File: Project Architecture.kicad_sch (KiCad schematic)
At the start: 0 parts

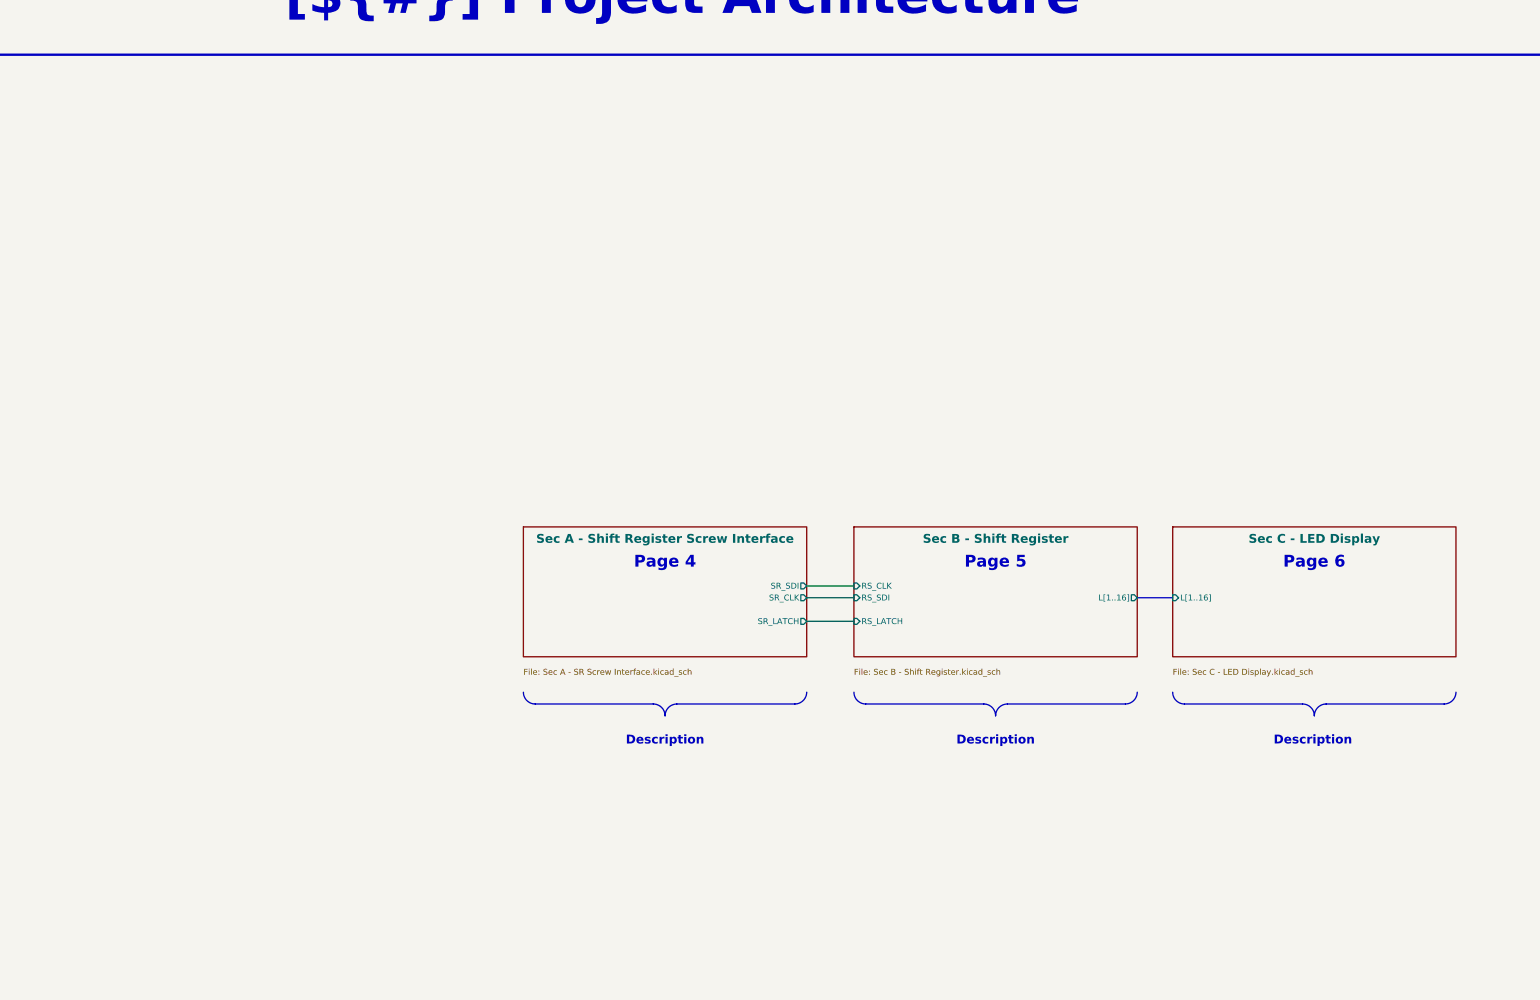
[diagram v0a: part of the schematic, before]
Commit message: documentation update / block diagram
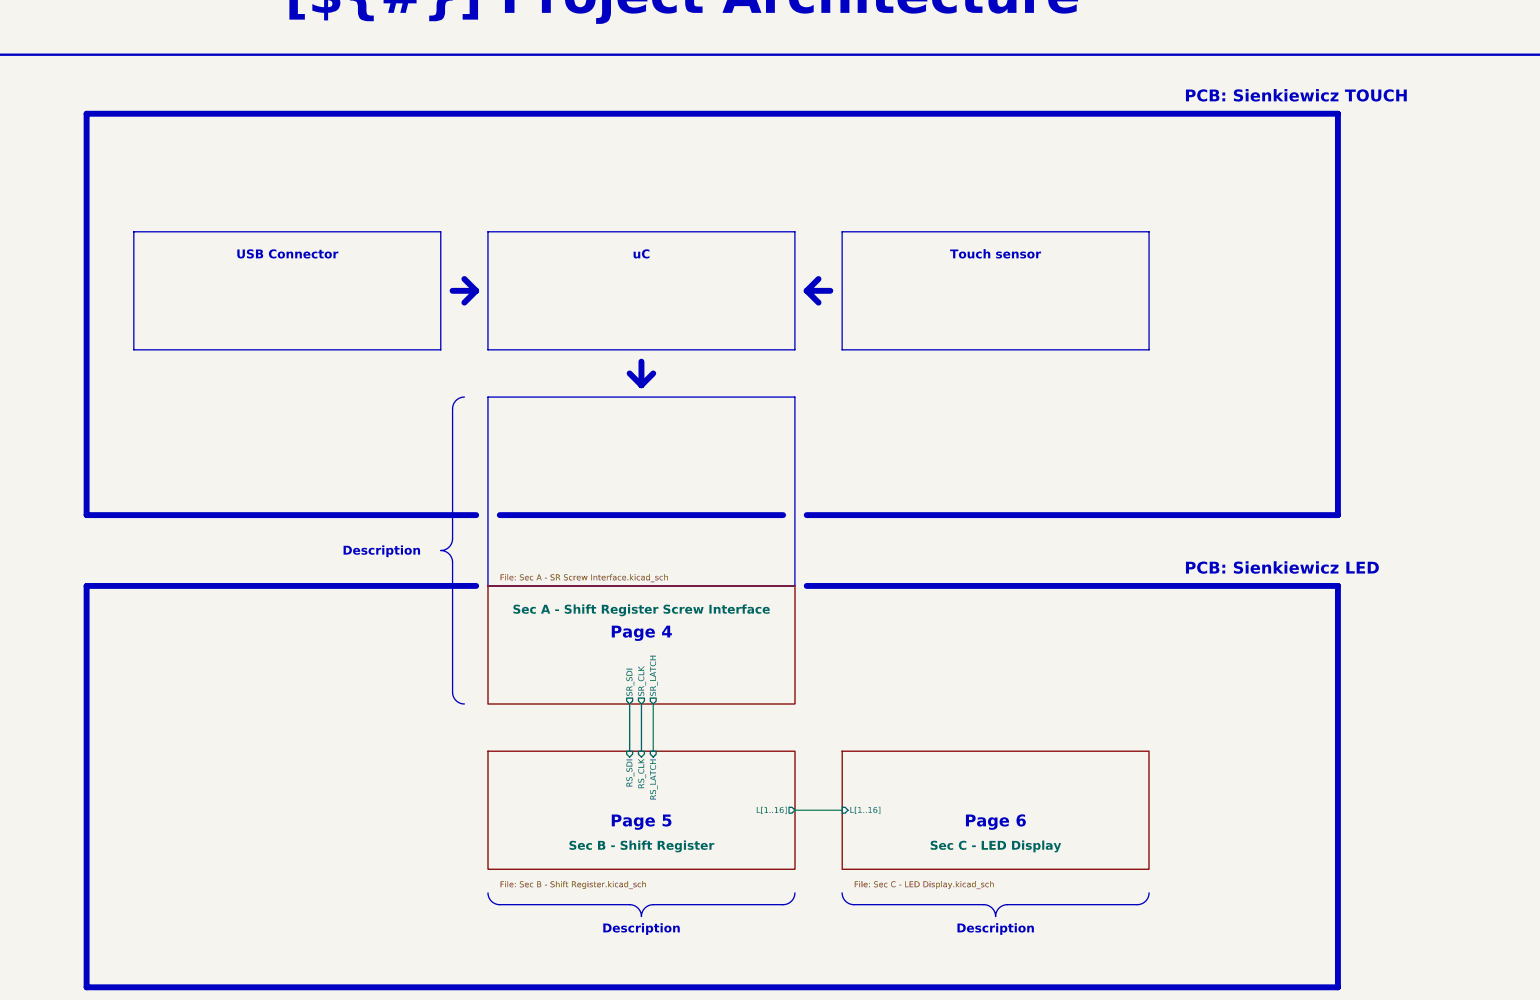
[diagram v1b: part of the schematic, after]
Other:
- note added: "PCB: Sienkiewicz LED"
- note added: "PCB: Sienkiewicz TOUCH"
- note added: "Touch sensor"
- note added: "USB Connector"
- note added: "uC"
